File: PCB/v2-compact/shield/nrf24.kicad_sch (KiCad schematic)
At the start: 0 parts

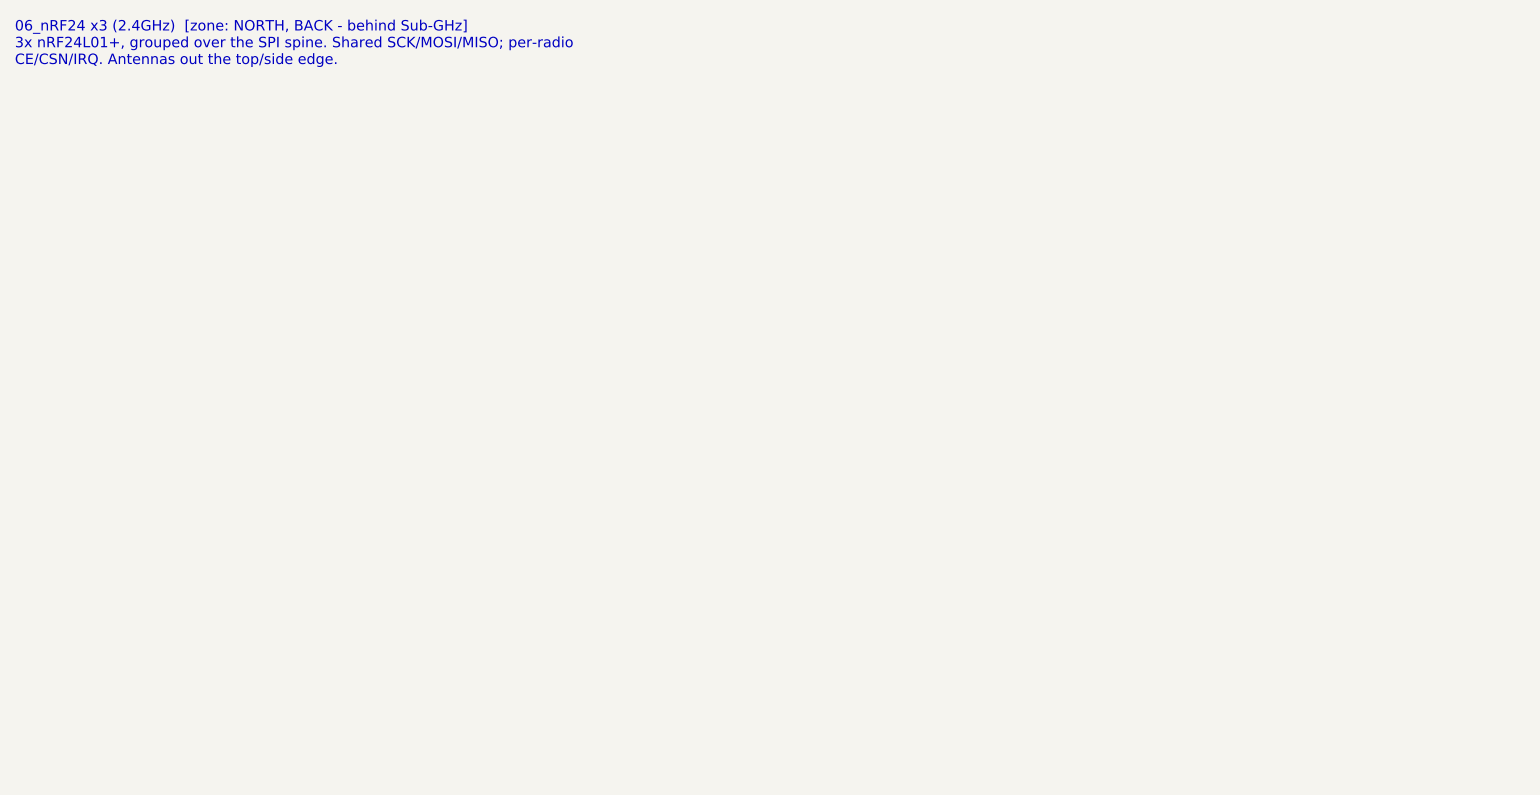
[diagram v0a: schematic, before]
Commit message: Schematics: custom symbols + footprint lib + backbone/nRF24/iButton sheets
- Add SnowOwl.kicad_sym (nRF24 + CC1101 module symbols; MISO tri-state for the
  shared SPI bus) and SnowOwl.pretty with the 2x10 stack-header footprint,
  registered via project sym-lib-table / fp-lib-table on both boards.
- Capture sheets, each netlist- and ERC-checked:
  - J1 stack header (both boards) wired to the locked pinout (the interconnect
    backbone: power + I2C + S3<->C5 UART + S3<->RV1106 UART + IR + 1-Wire)
  - nRF24 x3 on the shared SPI spine (per-radio CE/CSN/IRQ) with decoupling
  - iButton 1-Wire with pull-up
- Engine: snap all placements to the 1.27mm grid (clears 103 off-grid warnings);
  globally-unique power-symbol refs.

Remaining ERC items are expected for a partial design (isolated labels resolve
when both ends of a net are captured; power-not-driven clears with the power sheet).
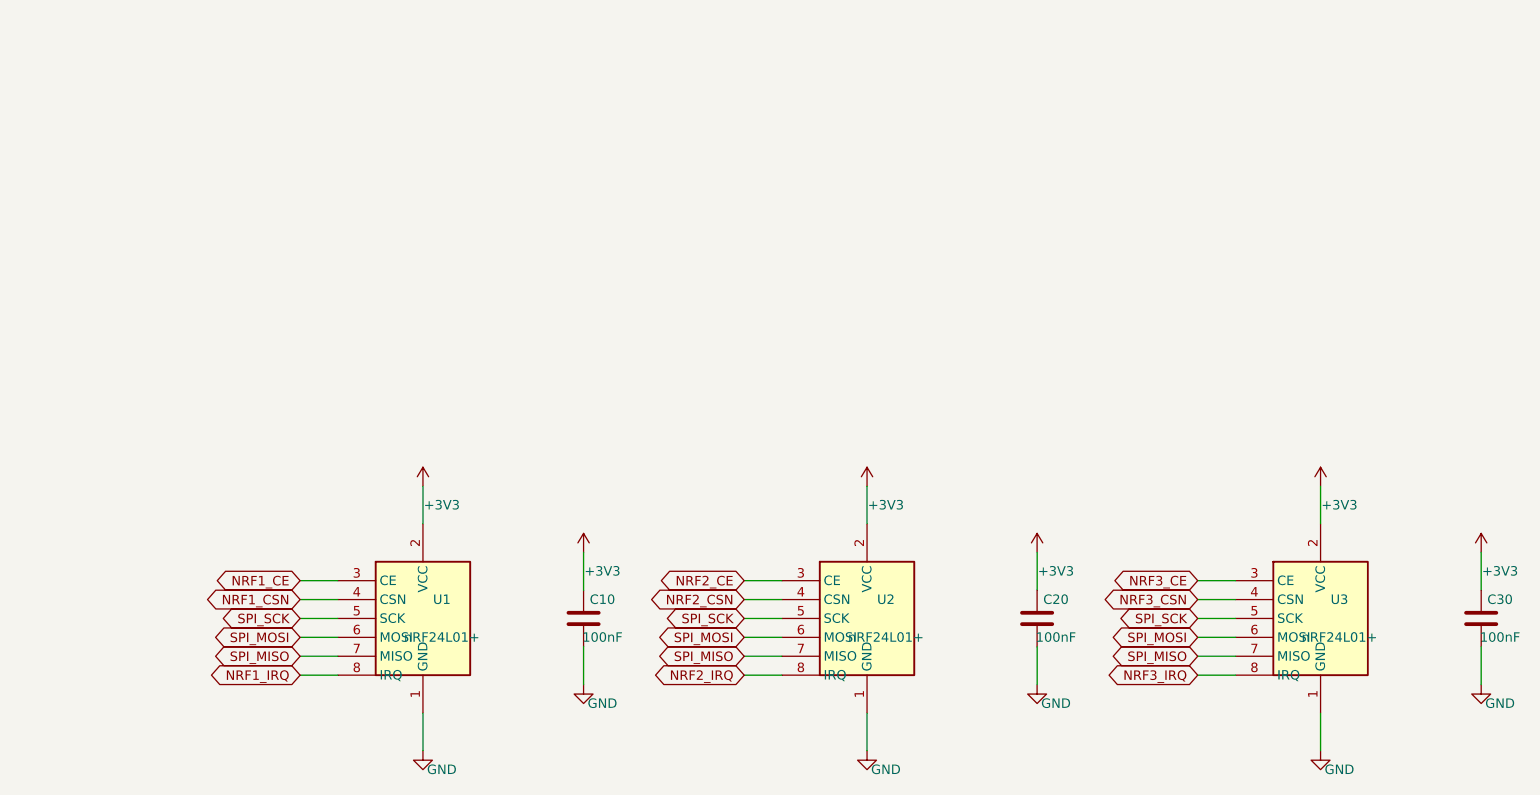
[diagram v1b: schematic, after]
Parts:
- added C10, C20, C30: 100nF, Capacitor_SMD:C_0402_1005Metric, symbol Device:C
- added U1, U2, U3: nRF24L01+, Connector_PinHeader_2.54mm:PinHeader_2x04_P2.54mm_Vertical, symbol SnowOwl:nRF24_Module
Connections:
- new net +3V3: C10.1, C20.1, C30.1, U1.2 (VCC), U2.2 (VCC), U3.2 (VCC)
- new net GND: C10.2, C20.2, C30.2, U1.1 (GND), U2.1 (GND), U3.1 (GND)
- new net NRF1_CE: U1.3 (CE)
- new net NRF1_CSN: U1.4 (CSN)
- new net NRF1_IRQ: U1.8 (IRQ)
- new net NRF2_CE: U2.3 (CE)
- new net NRF2_CSN: U2.4 (CSN)
- new net NRF2_IRQ: U2.8 (IRQ)
- new net NRF3_CE: U3.3 (CE)
- new net NRF3_CSN: U3.4 (CSN)
- new net NRF3_IRQ: U3.8 (IRQ)
- new net SPI_MISO: U1.7 (MISO), U2.7 (MISO), U3.7 (MISO)
- new net SPI_MOSI: U1.6 (MOSI), U2.6 (MOSI), U3.6 (MOSI)
- new net SPI_SCK: U1.5 (SCK), U2.5 (SCK), U3.5 (SCK)
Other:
- note removed: "06_nRF24 x3 (2.4GHz) [zone: NORTH, BACK - behind Sub-GHz] 3x nRF24L01+, grouped over the SPI spine. Shared SCK/MOSI/MISO; per-radio CE/CSN/IRQ. Antennas out the top/side edge."
